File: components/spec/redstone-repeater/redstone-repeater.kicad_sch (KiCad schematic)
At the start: 9 parts, among them Q13 Q_NMOS_DGS, Q14 Q_NMOS_DGS, Q15 Q_NMOS_DGS, Q16 Q_NMOS_DGS

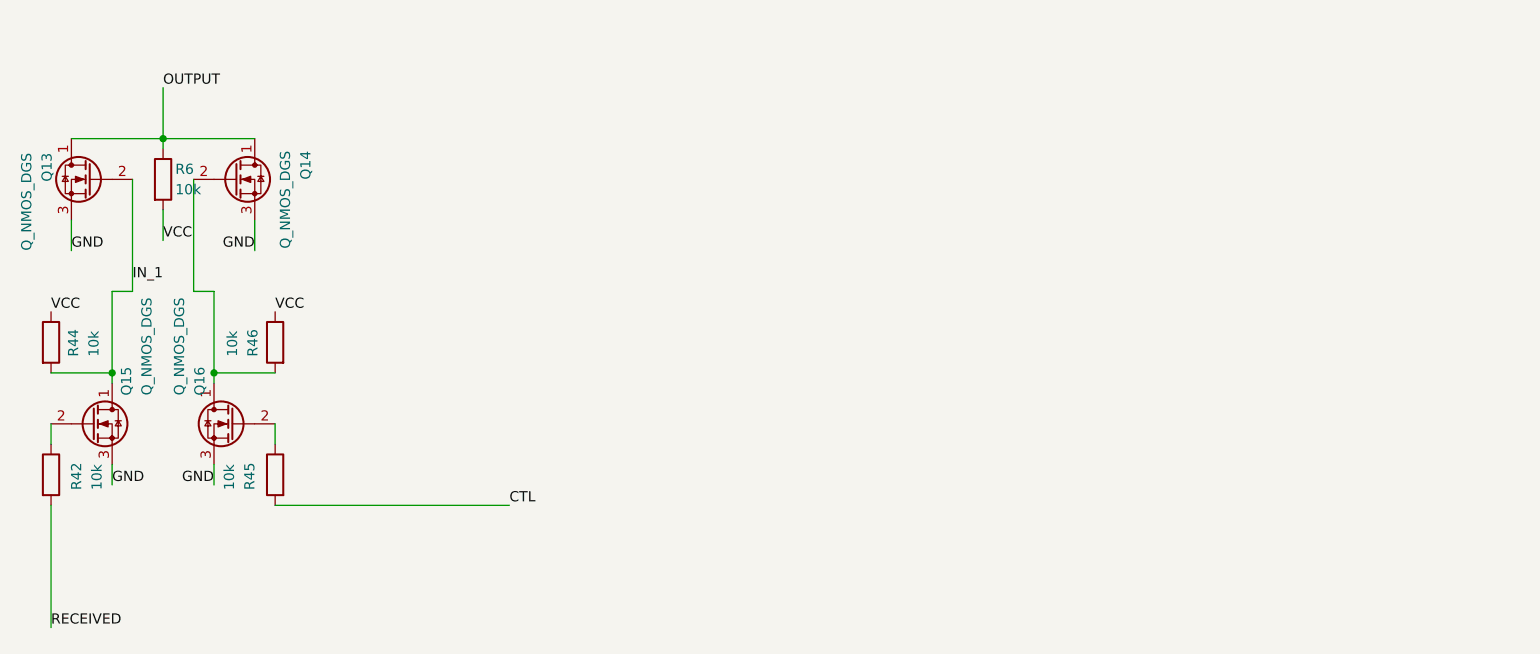
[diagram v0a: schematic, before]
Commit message: Change MOSFETs to NPN
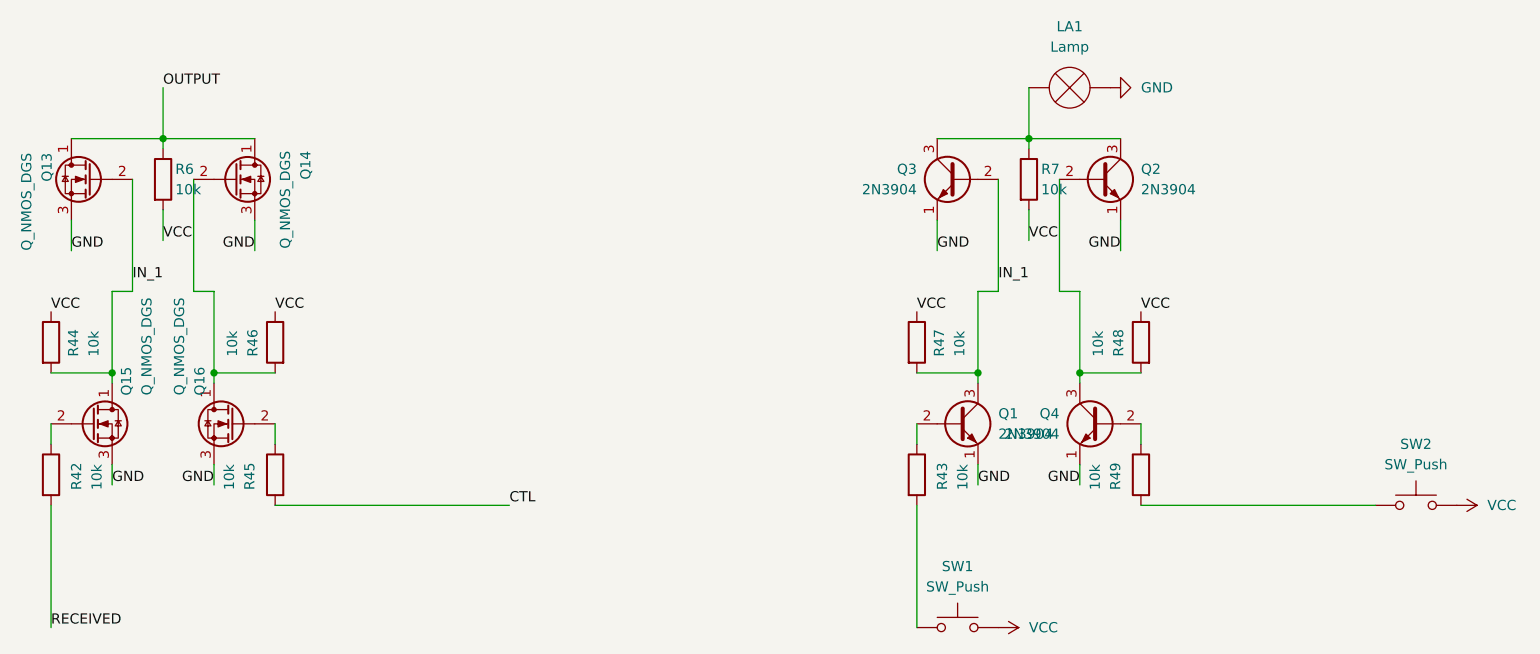
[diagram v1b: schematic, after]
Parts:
- added LA1: Lamp, symbol Device:Lamp
- added Q1, Q2, Q3, Q4: 2N3904, Package_TO_SOT_THT:TO-92_Inline, symbol Transistor_BJT:2N3904
- added R43, R47, R48, R49: 10k, Resistor_THT:R_Axial_DIN0207_L6.3mm_D2.5mm_P7.62mm_Horizontal, symbol Device:R
- added R7: 10k, symbol Device:R
- added SW1, SW2: SW_Push, symbol Switch:SW_Push
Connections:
- net GND: now also LA1.1 (-), Q1.1 (E), Q2.1 (E), Q3.1 (E), Q4.1 (E)
- net IN_1: now also Q1.3 (C), Q3.2 (B), R47.2
- net VCC: now also R47.1, R48.1, R7.2, SW1.2, SW2.2
- new net: Q1.2 (B), R43.1
- new net: R43.2, SW1.1
- new net: LA1.2 (+), Q2.3 (C), Q3.3 (C), R7.1
- new net: Q4.2 (B), R49.1
- new net: R49.2, SW2.1
- new net: Q2.2 (B), Q4.3 (C), R48.2
